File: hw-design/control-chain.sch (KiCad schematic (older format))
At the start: 37 parts, among them J1 RJ45_LEDS, J2 RJ45_LEDS, Q1 MMBT3904, Q2 MMBT3904, Q3 MMBT3904, Q4 MMBT3904, Q5 MMBT3906, U3 MAX13450E

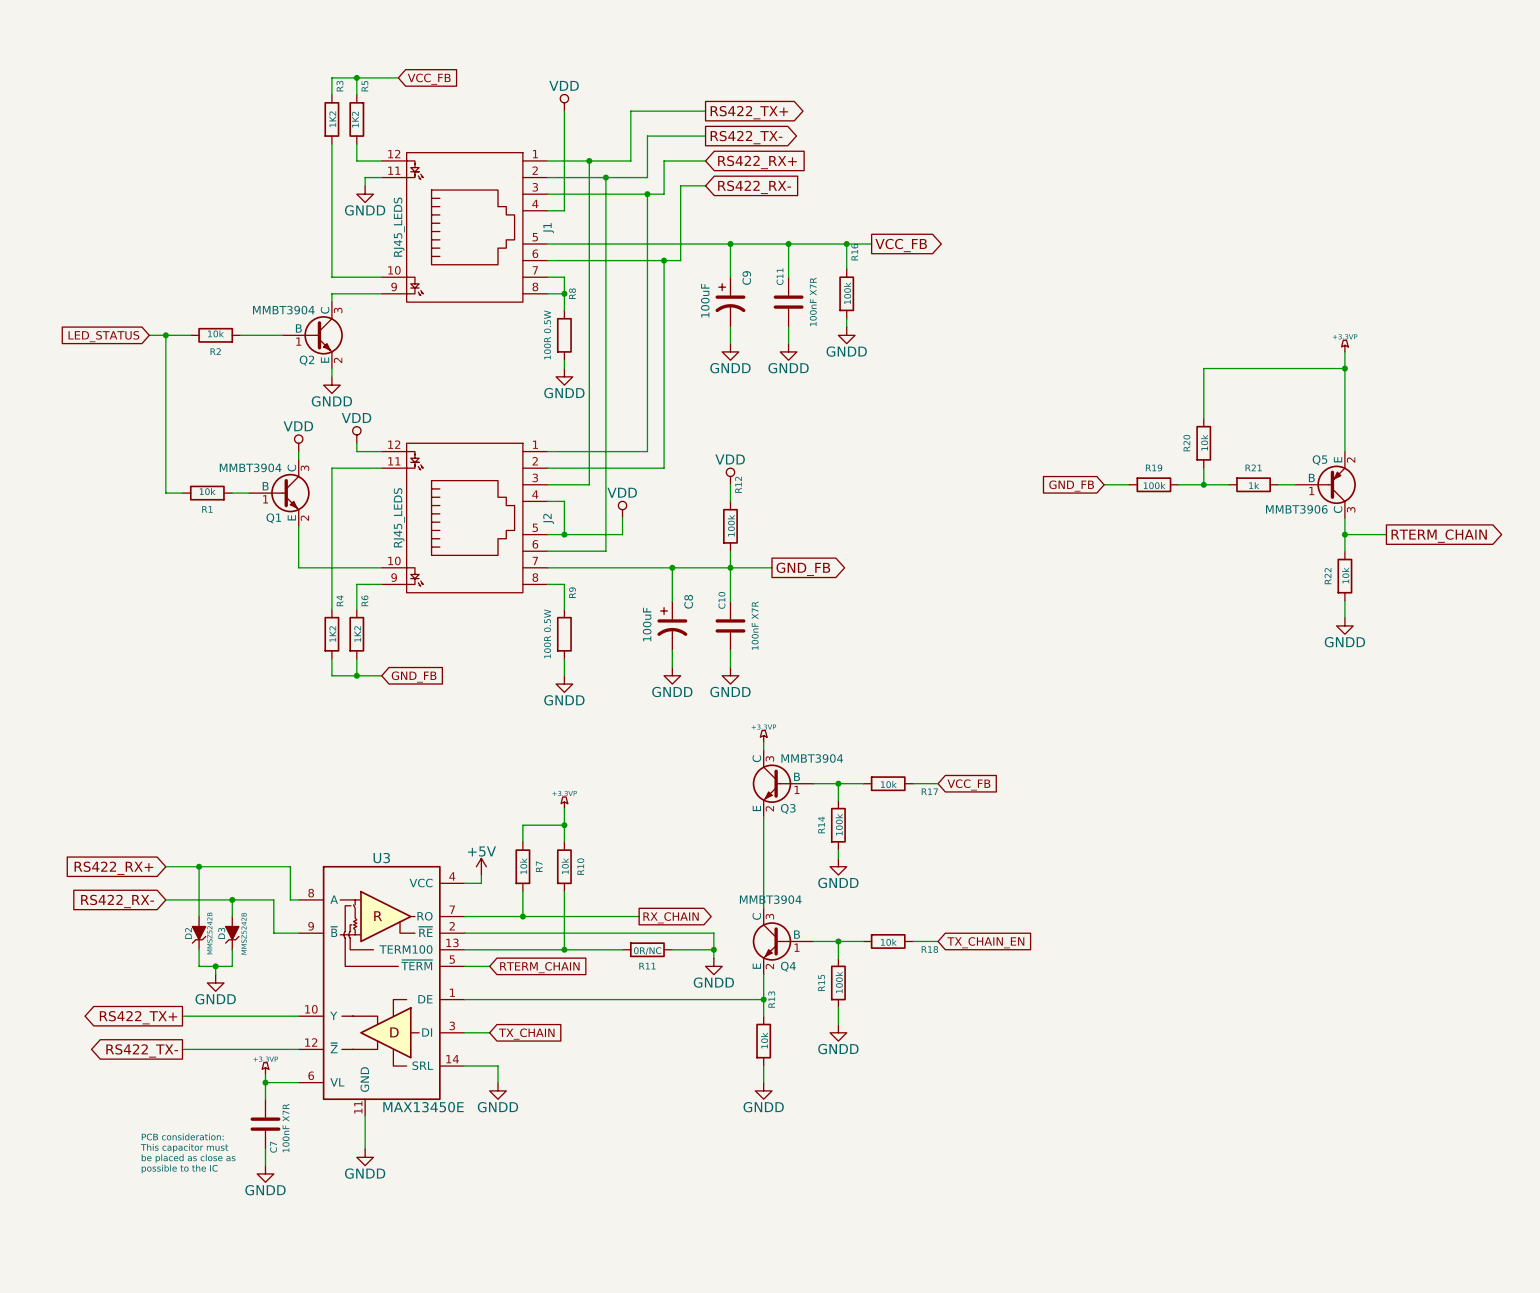
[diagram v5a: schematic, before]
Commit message: sch: updating some cached symbols
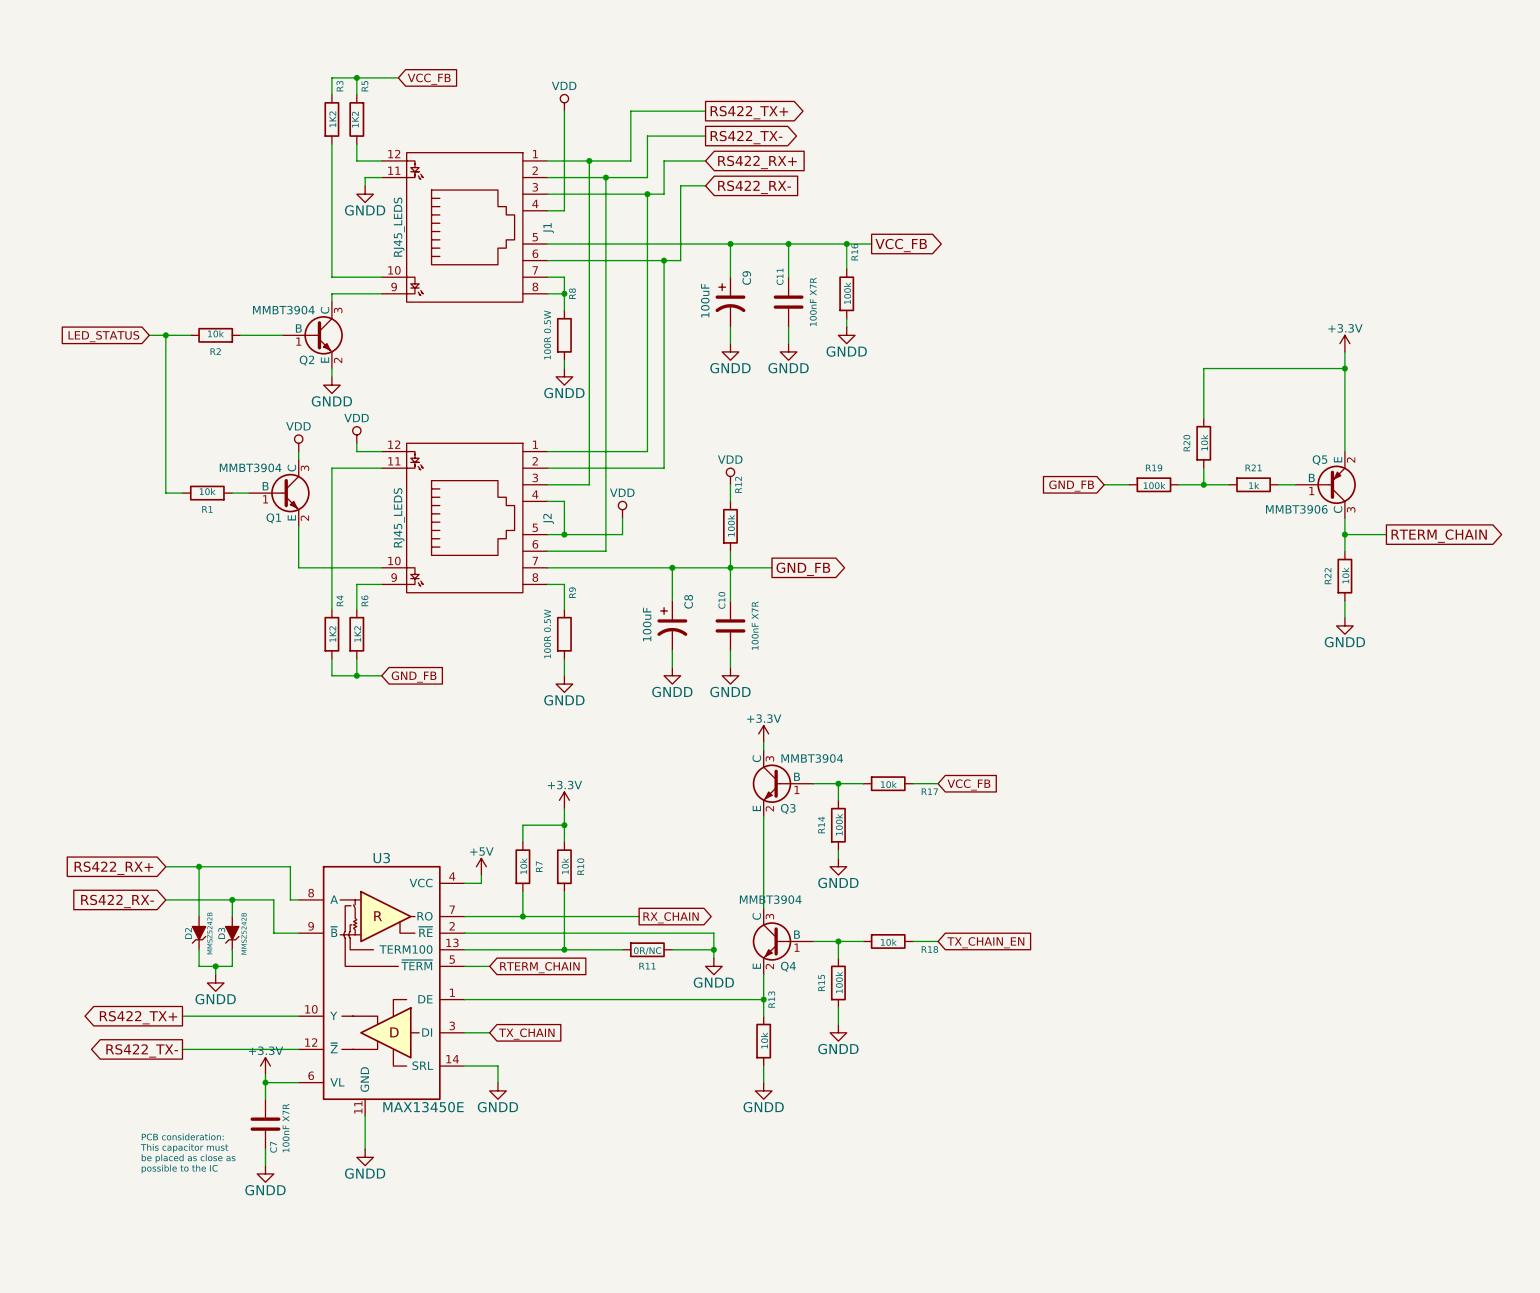
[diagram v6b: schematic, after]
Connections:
- net +3.3VP renamed +3V3
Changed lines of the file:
@@
 LIBS:conn
 LIBS:interface
-LIBS:expression-pedal-cache
 EELAYER 25 0
 EELAYER END
@@
 U 1 1 54EAA937
 P 3300 5700
-F 0 "#PWR029" H 3300 5550 60  0001 C CNN
-F 1 "+5V" H 3300 5840 60  0000 C CNN
+F 0 "#PWR029" H 3300 5550 50  0001 C CNN
+F 1 "+5V" H 3300 5840 50  0000 C CNN
 F 2 "" H 3300 5700 60  0000 C CNN
 F 3 "" H 3300 5700 60  0000 C CNN
@@
 	3300 5750 3300 5700
 $Comp
-L +3.3VP #PWR030
-U 1 1 54EAC962
-P 3800 5300
-F 0 "#PWR030" H 3850 5330 20  0001 C CNN
-F 1 "+3.3VP" H 3800 5390 30  0000 C CNN
-F 2 "" H 3800 5300 60  0000 C CNN
-F 3 "" H 3800 5300 60  0000 C CNN
-	1    3800 5300
-	1    0    0    -1
-$EndComp
-$Comp
-L +3.3VP #PWR031
-U 1 1 54EB1317
-P 5000 4900
-F 0 "#PWR031" H 5050 4930 20  0001 C CNN
-F 1 "+3.3VP" H 5000 4990 30  0000 C CNN
-F 2 "" H 5000 4900 60  0000 C CNN
-F 3 "" H 5000 4900 60  0000 C CNN
-	1    5000 4900
-	1    0    0    -1
-$EndComp
-$Comp
 L VDD #PWR032
 U 1 1 54EB4A3A
 P 2200 3150
-F 0 "#PWR032" H 2200 3000 60  0001 C CNN
-F 1 "VDD" H 2200 3300 60  0000 C CNN
+F 0 "#PWR032" H 2200 3000 50  0001 C CNN
+F 1 "VDD" H 2200 3300 50  0000 C CNN
 F 2 "" H 2200 3150 60  0000 C CNN
 F 3 "" H 2200 3150 60  0000 C CNN
@@
 U 1 1 54EB4B80
 P 2550 3100
-F 0 "#PWR033" H 2550 2950 60  0001 C CNN
-F 1 "VDD" H 2550 3250 60  0000 C CNN
+F 0 "#PWR033" H 2550 2950 50  0001 C CNN
+F 1 "VDD" H 2550 3250 50  0000 C CNN
 F 2 "" H 2550 3100 60  0000 C CNN
 F 3 "" H 2550 3100 60  0000 C CNN
@@
 U 1 1 54EB7074
 P 4150 3550
-F 0 "#PWR035" H 4150 3400 60  0001 C CNN
-F 1 "VDD" H 4150 3700 60  0000 C CNN
+F 0 "#PWR035" H 4150 3400 50  0001 C CNN
+F 1 "VDD" H 4150 3700 50  0000 C CNN
 F 2 "" H 4150 3550 60  0000 C CNN
 F 3 "" H 4150 3550 60  0000 C CNN
@@
 U 1 1 54EB756A
 P 4800 3350
-F 0 "#PWR036" H 4800 3200 60  0001 C CNN
-F 1 "VDD" H 4800 3500 60  0000 C CNN
+F 0 "#PWR036" H 4800 3200 50  0001 C CNN
+F 1 "VDD" H 4800 3500 50  0000 C CNN
 F 2 "" H 4800 3350 60  0000 C CNN
 F 3 "" H 4800 3350 60  0000 C CNN
@@
 $EndComp
 $Comp
-L +3.3VP #PWR041
-U 1 1 54EC40BA
-P 8500 2550
-F 0 "#PWR041" H 8550 2580 20  0001 C CNN
-F 1 "+3.3VP" H 8500 2640 30  0000 C CNN
-F 2 "" H 8500 2550 60  0000 C CNN
-F 3 "" H 8500 2550 60  0000 C CNN
-	1    8500 2550
-	1    0    0    -1
-$EndComp
-$Comp
 L GNDD #PWR042
 U 1 1 54EC472B
@@
 U 1 1 54ECB47D
 P 3800 1100
-F 0 "#PWR046" H 3800 950 60  0001 C CNN
-F 1 "VDD" H 3800 1250 60  0000 C CNN
+F 0 "#PWR046" H 3800 950 50  0001 C CNN
+F 1 "VDD" H 3800 1250 50  0000 C CNN
 F 2 "" H 3800 1100 60  0000 C CNN
 F 3 "" H 3800 1100 60  0000 C CNN
@@
 F 3 "" H 2600 1550 60  0000 C CNN
 	1    2600 1550
-	1    0    0    -1
-$EndComp
-$Comp
-L +3.3VP #PWR048
-U 1 1 54ED0001
-P 2000 6900
-F 0 "#PWR048" H 2050 6930 20  0001 C CNN
-F 1 "+3.3VP" H 2000 6990 30  0000 C CNN
-F 2 "" H 2000 6900 60  0000 C CNN
-F 3 "" H 2000 6900 60  0000 C CNN
-	1    2000 6900
 	1    0    0    -1
 $EndComp
@@
 Wire Wire Line
 	2400 2250 2400 2200
+$Comp
+L +3.3V #PWR?
+U 1 1 556F035A
+P 8500 2550
+F 0 "#PWR?" H 8500 2400 50  0001 C CNN
+F 1 "+3.3V" H 8500 2690 50  0000 C CNN
+F 2 "" H 8500 2550 60  0000 C CNN
+F 3 "" H 8500 2550 60  0000 C CNN
+	1    8500 2550
+	1    0    0    -1
+$EndComp
+$Comp
+L +3.3V #PWR?
+U 1 1 556F1F85
+P 3800 5300
+F 0 "#PWR?" H 3800 5150 50  0001 C CNN
+F 1 "+3.3V" H 3800 5440 50  0000 C CNN
+F 2 "" H 3800 5300 60  0000 C CNN
+F 3 "" H 3800 5300 60  0000 C CNN
+	1    3800 5300
+	1    0    0    -1
+$EndComp
+$Comp
+L +3.3V #PWR?
+U 1 1 556F1FBE
+P 5000 4900
+F 0 "#PWR?" H 5000 4750 50  0001 C CNN
+F 1 "+3.3V" H 5000 5040 50  0000 C CNN
+F 2 "" H 5000 4900 60  0000 C CNN
+F 3 "" H 5000 4900 60  0000 C CNN
+	1    5000 4900
+	1    0    0    -1
+$EndComp
+$Comp
+L +3.3V #PWR?
+U 1 1 556F61AF
+P 2000 6900
+F 0 "#PWR?" H 2000 6750 50  0001 C CNN
+F 1 "+3.3V" H 2000 7040 50  0000 C CNN
+F 2 "" H 2000 6900 60  0000 C CNN
+F 3 "" H 2000 6900 60  0000 C CNN
+	1    2000 6900
+	1    0    0    -1
+$EndComp
 $EndSCHEMATC
